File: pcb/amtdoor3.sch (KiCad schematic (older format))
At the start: 45 parts, among them P1 CONN_01X03, P2 dnp-REF-182665-01, P3 CONN_01X03, P4 CONN_01X04, P5 CONN_01X02, P6 CONN_01X02, Q1 Q_NMOS_GSD, Q2 Q_PMOS_HP, Q3 DMMT3906_Dual_PNP, Q4 Q_NMOS_GSD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

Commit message: new rev schematic updates and footprint grouping
* change level shifter to NFET gates w/ pull up b/c NVT2002 leaks 5V EN to 3.3V rail
* add selectable, fused output voltage to each port
* rename P2 to P4 so the output ports are P1, P2, P3
* use level shifting on all ports
* reassign GPIO to ports so we have UART TX+RX, PWM, and plain GPIO
* add fuses and DNPs so boost and buck can be populated but not interfere
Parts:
- removed C3, C5: 0.1uF, Capacitors_SMD:C_0805, symbol C_Small
- removed P1, P3: CONN_01X03, Socket_Strips:Socket_Strip_Straight_1x03, symbol CONN_01X03
- removed Q1, Q4: Q_NMOS_GSD, TO_SOT_Packages_SMD:SOT-23, symbol Q_NMOS_GSD
- removed U2: NVT2002, Housings_SSOP:TSSOP-8_3x3mm_Pitch0.65mm, symbol NVT2002
- added D3, D4, D5, D8, D9: LED Green, LEDs:LED_0603, symbol Led_Small
- added F1: 250mA, Resistors_SMD:R_1206, symbol F_Small
- added F2, F3, F4, F5, F6, F7: F_Small, Resistors_SMD:R_0603, symbol F_Small
- added F8: 500mA, Resistors_SMD:R_1206, symbol F_Small
- added P1, P3: CONN_01X04, Socket_Strips:Socket_Strip_Straight_1x04, symbol CONN_01X04
- added Q1, Q10, Q5, Q6, Q7, Q8, Q9: Q_NMOS_DUAL, TO_SOT_Packages_SMD:SOT-23-6, symbol Q_NMOS_DUAL
- added Q4: Q_PMOS_GSD, TO_SOT_Packages_SMD:SOT-23, symbol Q_PMOS_GSD
- added R15, R21, R22, R23, R25: 1k, Resistors_SMD:R_0603, symbol R_Small
- added R16, R17, R18, R19, R20: 10k, Resistors_SMD:R_0603, symbol R_Small
- C1, C2, C6: footprint Capacitors_SMD:C_0805 -> Capacitors_SMD:C_0603; Type (none) -> SMT
- C4: value 4.7uF -> 4.7uF 25V; footprint Capacitors_SMD:C_0805 -> Capacitors_SMD:C_0603; Type (none) -> SMT
- C8: value 22uF -> 22uF 10V; Type (none) -> SMT
- D1: value 10BQ015 -> 15V 1A; Description (none) -> Diode Schottky 15V 1A Surface Mount DO-214AA (SMB); Digikey Part No (none) -> VS-10BQ015-M3/5BTGICT-ND; Mfg (none) -> Vishay Semiconductor; Mfg Part No (none) -> VS-10BQ015-M3/5BT; Type (none) -> SMT
- D2, D6, D7: footprint LEDs:LED_0805 -> LEDs:LED_0603
- L1, U1, U3: Type (none) -> SMT
- L2: Description (none) -> 10µH Shielded Wirewound Inductor 2.5A 61.1 mOhm Max Nonstan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; Digikey Part No (none) -> 587-2081-1-ND; Mfg (none) -> Taiyo Yuden; Mfg Part No (none) -> NR6045T100M; Type (none) -> SMT
- P4: Type (none) -> TH
- P5, P6: Description (none) -> 2 Position Wire to Board Terminal Block Horizontal with Boa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; Digikey Part No (none) -> ED2740-ND; Mfg (none) -> On Shore Technology, Inc.; Mfg Part No (none) -> OSTTE020104; Type (none) -> TH
- Q2: Alt Mfg (none) -> Diodes Inc; Alt Mfg Part No (none) -> DMP3085LSS-13; Description (none) -> MOSFET P-CH 30V 7.3A 8SOIC; Digikey Part No (none) -> DMG4435SSS-13DICT-ND; Mfg (none) -> Diodes Inc; Mfg Part No (none) -> DMG4435SSS-13; Type (none) -> SMT
- Q3: Digikey Part No (none) -> DMMT3906-7-FDICT-ND; Mfg (none) -> Diodes Inc; Mfg Part No (none) -> DMMT3906-7-F; Type (none) -> SMT
- R1, R10, R11, R12, R2, R6, R7, R8, R9: footprint Resistors_SMD:R_0805 -> Resistors_SMD:R_0603; Type (none) -> SMT
- R13: value 1k -> 10k; footprint Resistors_SMD:R_0805 -> Resistors_SMD:R_0603
- R14, R24: footprint Resistors_SMD:R_0805 -> Resistors_SMD:R_0603
- R3: value 10k -> 1k; footprint Resistors_SMD:R_0805 -> Resistors_SMD:R_0603; Type (none) -> SMT
- R4: footprint Resistors_SMD:R_0805 -> Resistors_SMD:R_0603; Pop (none) -> DNP
- R5: value dnp -> 10k; footprint Resistors_SMD:R_0805 -> Resistors_SMD:R_0603; Type (none) -> SMT
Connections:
- net labels added: BST_FB, BST_SW, P12V_SW, P5V_BST, PORT2-1, PORT2-2, PORT3-1, PORT3-2, SW_D, VPORT1, VPORT2, VPORT3
- net labels removed: +3V3, FB_12V, GPIO20, SW_12V, VAUX, VSWITCHED, VSWITCHED_T, VSW_D
- wire segments 178 -> 265
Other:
- note added: "12-24V Indicators\n\n\n\n"
- note added: "5V Buck Regulator\n\n5V/500mA from 12-24V source for high voltage IO.\nShould only be used with the aux input (P6)"
- note added: "HV GPIO Indicators"
- note added: "HV GPIO w/ Level Shifting to 5V or 12-24V"
- note added: "Must use RPi pull ups!"
- note added: "PWM0/PWM1"
- note added: "UART"
- note added: "Use RPi PU"
- note removed: "5V Buck Regulator\n\n5V/500mA from 12-24V source for high voltage IO.\nShould only be used with the VAUX input."
- note removed: "Level Shifting\n\nRFID reader requires 5V supply/logic."
- note removed: "Switches/GPIO\n\nConfigure for ground/input\nwith pull-up."
- moved on the sheet: D2, D7, P4, R14, R24

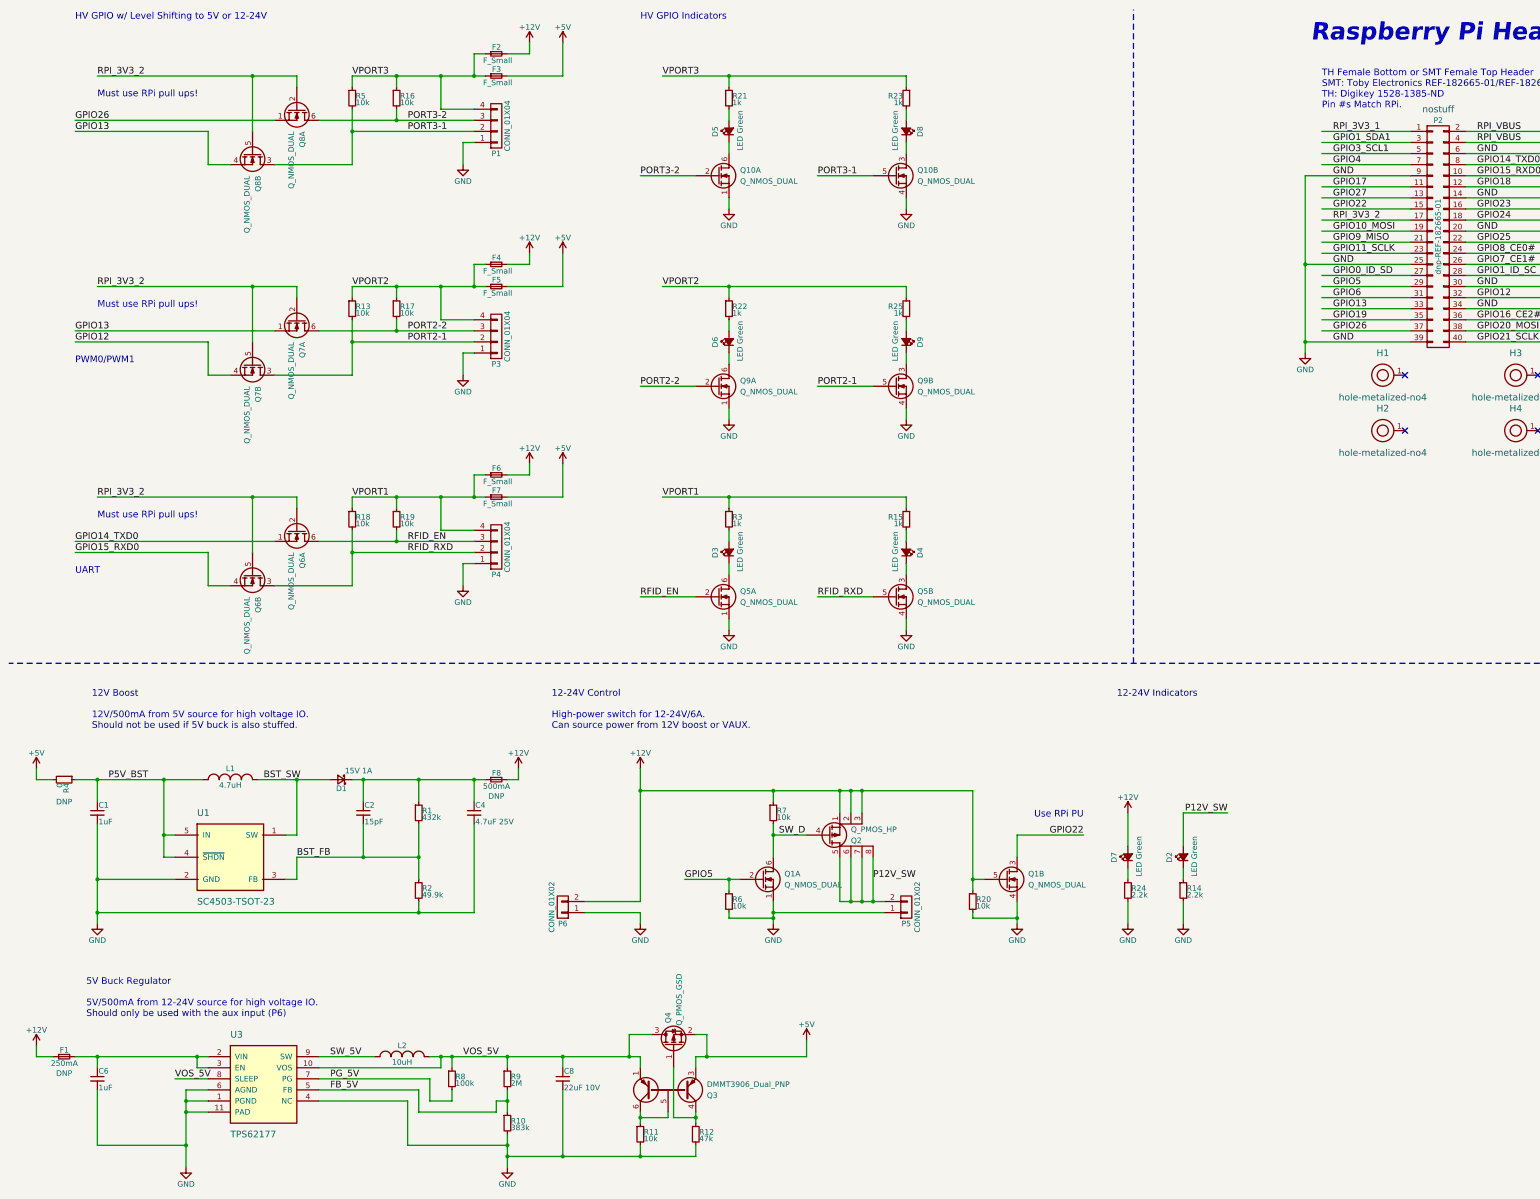
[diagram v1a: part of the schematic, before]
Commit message: new rev layout complete w/ some sch changes to help routing
* normalize boost net names
* fix boost part number to TPS62175. TPS62177 is fixed 3.3V
* DNP one option for output port voltage
* fix cap + voltage of boost/buck 12/24V decoupling caps C3, C4, C6
* reassign GPIO to ports to help routing
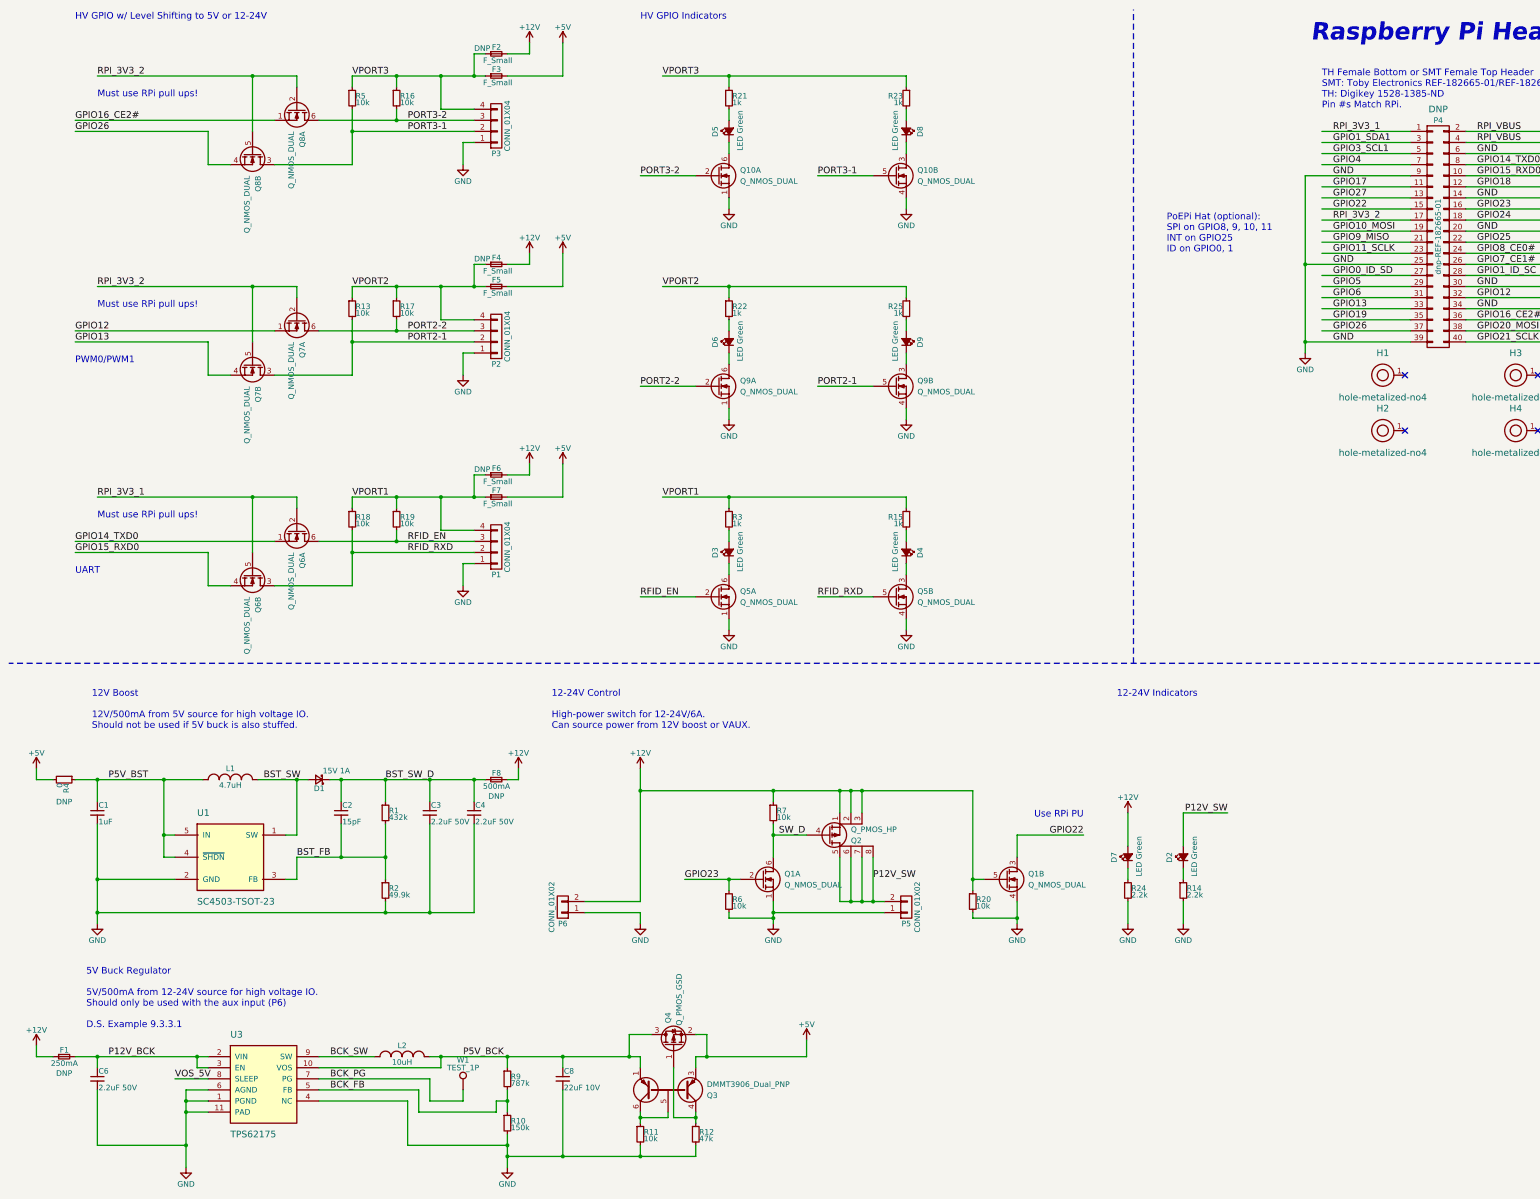
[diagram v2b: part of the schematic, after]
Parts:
- removed R8: 100k, Resistors_SMD:R_0603, symbol R_Small
- added C3: 2.2uF 50V, Capacitors_SMD:C_0805, symbol C_Small
- added W1: TEST_1P, Measurement_Points:Measurement_Point_Round-SMD-Pad_Small, symbol TEST_1P
- C4: value 4.7uF 25V -> 2.2uF 50V; footprint Capacitors_SMD:C_0603 -> Capacitors_SMD:C_0805
- C6: value 1uF -> 2.2uF 50V; footprint Capacitors_SMD:C_0603 -> Capacitors_SMD:C_0805
- C8: footprint Capacitors_SMD:C_1206 -> Capacitors_SMD:C_0805
- F1, F8: footprint Resistors_SMD:R_1206 -> Resistors_SMD:R_0805
- F2, F4, F6: Pop (none) -> DNP
- P4: renamed from P2; Pop (none) -> DNP; Type nostuff -> (none)
- R10: value 383k -> 150k
- R9: value 2M -> 787k
- U3: value TPS62177 -> TPS62175; Digikey Part No 296-41856-1-ND -> todo; Mfg Part No TPS62177DQCR -> todo
- renumbered P4 to P1, P3 to P2, P1 to P3
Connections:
- net labels added: BCK_FB, BCK_PG, BCK_SW, BST_SW_D, P12V_BCK, P5V_BCK
- net labels removed: FB_5V, PG_5V, SW_5V
- wire segments 265 -> 266
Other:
- note added: "5V Buck Regulator\n\n5V/500mA from 12-24V source for high voltage IO.\nShould only be used with the aux input (P6)\n\nD.S. Example 9.3.3.1"
- note added: "PoEPi Hat (optional): \nSPI on GPIO8, 9, 10, 11\nINT on GPIO25\nID on GPIO0, 1"
- note removed: "5V Buck Regulator\n\n5V/500mA from 12-24V source for high voltage IO.\nShould only be used with the aux input (P6)"
- moved on the sheet: C2, D1, R1, R2

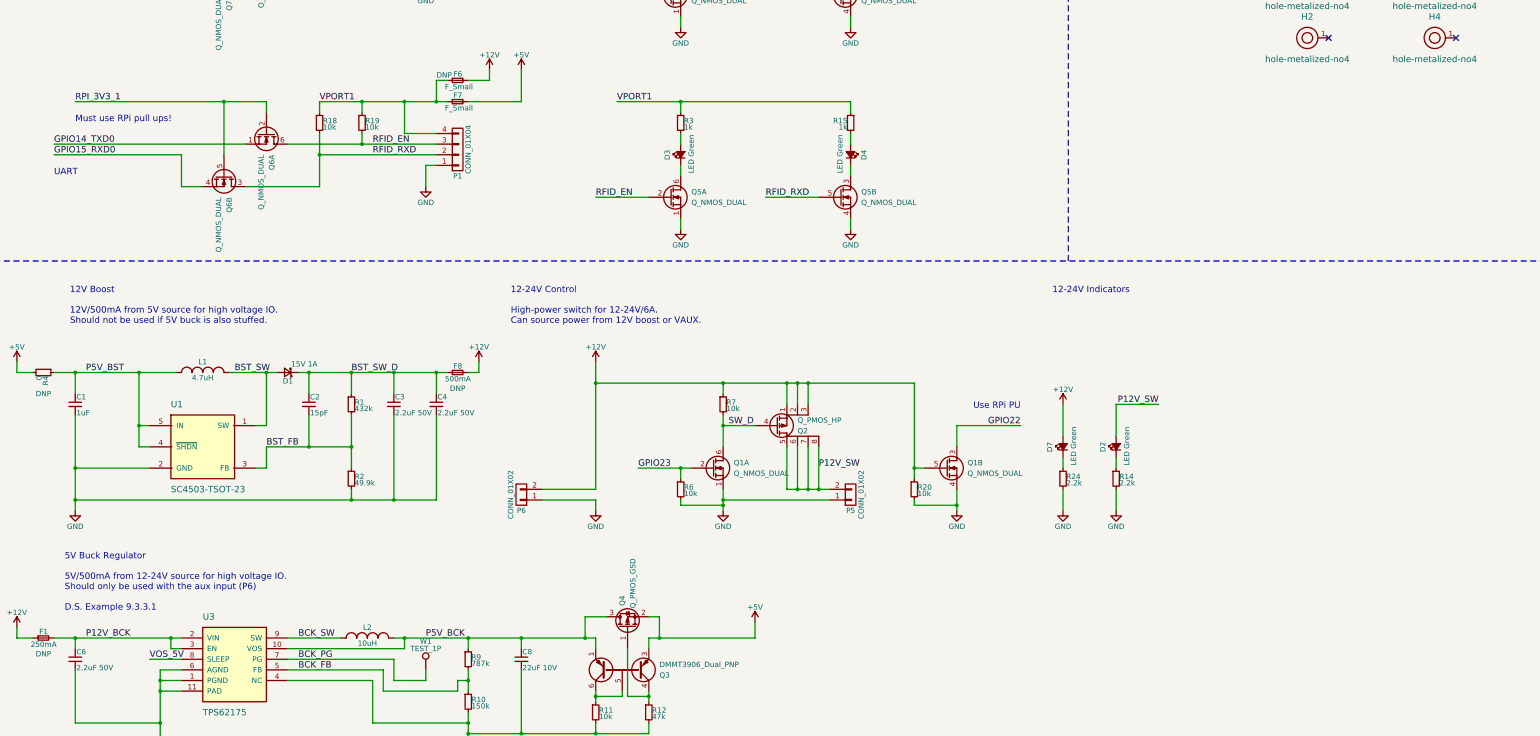
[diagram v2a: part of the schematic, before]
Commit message: pcb rev 2.0 gerbers, silk logos, routing tweaks
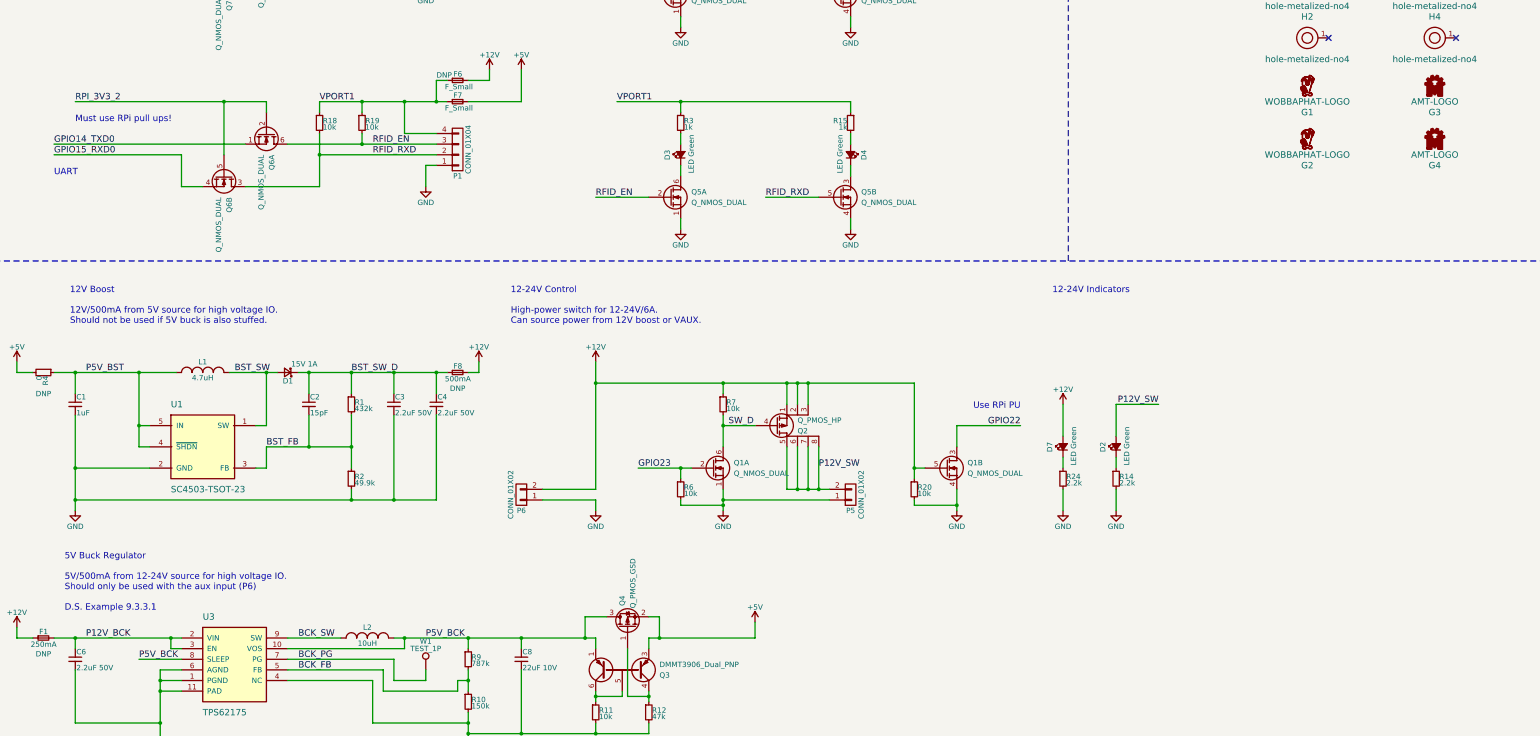
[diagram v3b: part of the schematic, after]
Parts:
- added G1: WOBBAPHAT-LOGO, amtdoor3:wobbaphat-logo-fcu, symbol WOBBAPHAT-LOGO
- added G2: WOBBAPHAT-LOGO, amtdoor3:wobbaphat-logo-fsilk-lg, symbol WOBBAPHAT-LOGO
- added G3: AMT-LOGO, amtdoor3:amt-logo-fcu, symbol AMT-LOGO
- added G4: AMT-LOGO, amtdoor3:amt-logo-fsilk-lg, symbol AMT-LOGO
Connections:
- net labels removed: VOS_5V
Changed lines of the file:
@@
 Text Notes 5400 7000 0    60   ~ 0
 12-24V Control\n\nHigh-power switch for 12-24V/6A.\nCan source power from 12V boost or VAUX.
-Text Label 2000 10150 0    60   ~ 0
-VOS_5V
+Text Label 1900 10150 0    60   ~ 0
+P5V_BCK
 $Comp
 L +5V #PWR013
@@
 	3300 9950 3800 9950
 Wire Wire Line
-	5500 10050 5500 9950
+	5500 9950 5500 10050
 Connection ~ 5500 9950
 Wire Wire Line
-	5000 10050 5000 9950
+	5000 9950 5000 10050
 Connection ~ 5000 9950
 Wire Wire Line
@@
 	2300 10050 2200 10050
 Wire Wire Line
-	2200 10050 2200 9950
+	2200 9950 2200 10050
 Connection ~ 2200 9950
 Wire Wire Line
-	2300 10150 2000 10150
+	2300 10150 1900 10150
 Wire Wire Line
 	6200 10450 6200 10550
@@
 	6300 9750 6100 9750
 Wire Wire Line
-	6100 9750 6100 9950
+	6100 9950 6100 9750
 Connection ~ 6100 9950
 Wire Wire Line
@@
 	1300 4900 3100 4900
 Text Label 1300 4900 0    60   ~ 0
-RPI_3V3_1
+RPI_3V3_2
 Wire Wire Line
 	2700 4900 2700 5400
@@
 Text Notes 10950 2700 0    60   ~ 0
 PoEPi Hat (optional): \nSPI on GPIO8, 9, 10, 11\nINT on GPIO25\nID on GPIO0, 1
+$Comp
+L WOBBAPHAT-LOGO G1
+U 1 1 59C86ADE
+P 12900 4750
+F 0 "G1" H 12900 4500 60  0000 C CNN
+F 1 "WOBBAPHAT-LOGO" H 12900 4600 60  0000 C CNN
+F 2 "amtdoor3:wobbaphat-logo-fcu" H 12900 4750 60  0001 C CNN
+F 3 "" H 12900 4750 60  0000 C CNN
+	1    12900 4750
+	1    0    0    -1
+$EndComp
+$Comp
+L WOBBAPHAT-LOGO G2
+U 1 1 59C86CF7
+P 12900 5250
+F 0 "G2" H 12900 5000 60  0000 C CNN
+F 1 "WOBBAPHAT-LOGO" H 12900 5100 60  0000 C CNN
+F 2 "amtdoor3:wobbaphat-logo-fsilk-lg" H 12900 5250 60  0001 C CNN
+F 3 "" H 12900 5250 60  0000 C CNN
+	1    12900 5250
+	1    0    0    -1
+$EndComp
+$Comp
+L AMT-LOGO G3
+U 1 1 59C86DB8
+P 14100 4750
+F 0 "G3" H 14100 4500 60  0000 C CNN
+F 1 "AMT-LOGO" H 14100 4600 60  0000 C CNN
+F 2 "amtdoor3:amt-logo-fcu" H 14100 4750 60  0001 C CNN
+F 3 "" H 14100 4750 60  0000 C CNN
+	1    14100 4750
+	1    0    0    -1
+$EndComp
+$Comp
+L AMT-LOGO G4
+U 1 1 59C86E78
+P 14100 5250
+F 0 "G4" H 14100 5000 60  0000 C CNN
+F 1 "AMT-LOGO" H 14100 5100 60  0000 C CNN
+F 2 "amtdoor3:amt-logo-fsilk-lg" H 14100 5250 60  0001 C CNN
+F 3 "" H 14100 5250 60  0000 C CNN
+	1    14100 5250
+	1    0    0    -1
+$EndComp
 $EndSCHEMATC
